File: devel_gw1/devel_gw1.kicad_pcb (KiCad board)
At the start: 4 copper layers, 50.8 x 95.2 mm, 179 parts, among them Q1 2N7002, Q10 2N7002, Q11 2N7002, Q12 2N7002, Q13 2N7002, Q14 2N7002, Q15 2N7002, Q16 2N7002, Q17 2N7002, Q18 2N7002, Q19 2N7002, Q2 2N7002, Q20 2N7002, Q21 2N7002, Q22 2N7002, Q23 2N7002, Q24 2N7002, Q25 2N7002, Q26 2N7002, Q27 2N7002, Q28 2N7002, Q29 2N7002, Q3 2N7002, Q30 2N7002, Q31 2N7002, Q32 2N7002, Q33 2N7002, Q34 2N7002, Q35 2N7002, Q36 2N7002, Q37 2N7002, Q38 2N7002, Q39 2N7002, Q4 2N7002, Q41 2N7002, Q5 2N7002, Q6 2N7002, Q7 2N7002, Q8 2N7002, Q9 2N7002, U1 GW1N-LV9QN88C6_I5_, U2 LM3480-3.3, U3 AP2202K-ADJ, U4 ESP-PSRAM32, U5 AT25SF081-XMHF-X, U6 AP62150Z6, X1 ASE-xxxMHz

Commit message: Devel board is production ready
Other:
- copper layers 4 -> 2
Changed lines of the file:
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@@
   (layers
     (0 "F.Cu" signal)
-    (1 "In1.Cu" mixed)
-    (2 "In2.Cu" mixed)
     (31 "B.Cu" signal)
     (32 "B.Adhes" user "B.Adhesive")
@@
       (layer "F.Mask" (type "Top Solder Mask") (thickness 0.01))
       (layer "F.Cu" (type "copper") (thickness 0.035))
-      (layer "dielectric 1" (type "core") (thickness 0.48) (material "FR4") (epsilon_r 4.5) (loss_tangent 0.02))
-      (layer "In1.Cu" (type "copper") (thickness 0.035))
-      (layer "dielectric 2" (type "prepreg") (thickness 0.48) (material "FR4") (epsilon_r 4.5) (loss_tangent 0.02))
-      (layer "In2.Cu" (type "copper") (thickness 0.035))
-      (layer "dielectric 3" (type "core") (thickness 0.48) (material "FR4") (epsilon_r 4.5) (loss_tangent 0.02))
+      (layer "dielectric 1" (type "core") (thickness 1.51) (material "FR4") (epsilon_r 4.5) (loss_tangent 0.02))
       (layer "B.Cu" (type "copper") (thickness 0.035))
       (layer "B.Mask" (type "Bottom Solder Mask") (thickness 0.01))
@@
     (grid_origin 144.7 83.3)
     (pcbplotparams
-      (layerselection 0x00010fc_ffffffff)
+      (layerselection 0x00010e0_ffffffff)
       (plot_on_all_layers_selection 0x0000000_00000000)
       (disableapertmacros false)
@@
       (outputformat 1)
       (mirror false)
-      (drillshape 1)
+      (drillshape 0)
       (scaleselection 1)
-      (outputdirectory "")
+      (outputdirectory "release-v1/")
     )
   )
@@
     (fp_line (start 1 0.625) (end -1 0.625)
       (stroke (width 0.1) (type solid)) (layer "F.Fab"))
-    (pad "1" smd roundrect (at -1.0375 0 180) (size 1.175 1.45) (layers "F.Cu" "F.Paste" "F.Mask") (roundrect_rratio 0.212766)
+    (pad "1" smd roundrect (at -1.0375 0 180) (size 1.175 1.45) (layers "F.Cu" "F.Paste" "F.Mask") (roundrect_rratio 0.2127659574)
       (net 129 "/V_IN") (pintype "passive"))
-    (pad "2" smd roundrect (at 1.0375 0 180) (size 1.175 1.45) (layers "F.Cu" "F.Paste" "F.Mask") (roundrect_rratio 0.212766)
+    (pad "2" smd roundrect (at 1.0375 0 180) (size 1.175 1.45) (layers "F.Cu" "F.Paste" "F.Mask") (roundrect_rratio 0.2127659574)
       (net 1 "GND") (pintype "passive"))
     (model "${KICAD6_3DMODEL_DIR}/Capacitor_SMD.3dshapes/C_0805_2012Metric.wrl"
@@
     (fp_line (start 1 0.625) (end -1 0.625)
       (stroke (width 0.1) (type solid)) (layer "F.Fab"))
-    (pad "1" smd roundrect (at -1.0375 0 270) (size 1.175 1.45) (layers "F.Cu" "F.Paste" "F.Mask") (roundrect_rratio 0.212766)
+    (pad "1" smd roundrect (at -1.0375 0 270) (size 1.175 1.45) (layers "F.Cu" "F.Paste" "F.Mask") (roundrect_rratio 0.2127659574)
       (net 117 "Net-(JP3-A)") (pintype "passive"))
-    (pad "2" smd roundrect (at 1.0375 0 270) (size 1.175 1.45) (layers "F.Cu" "F.Paste" "F.Mask") (roundrect_rratio 0.212766)
+    (pad "2" smd roundrect (at 1.0375 0 270) (size 1.175 1.45) (layers "F.Cu" "F.Paste" "F.Mask") (roundrect_rratio 0.2127659574)
       (net 1 "GND") (pintype "passive"))
     (model "${KICAD6_3DMODEL_DIR}/Capacitor_SMD.3dshapes/C_0805_2012Metric.wrl"
@@
     (fp_line (start 1.25 1) (end -1.25 1)
       (stroke (width 0.1) (type solid)) (layer "F.Fab"))
-    (pad "1" smd roundrect (at -1.1625 0 90) (size 1.425 2.2) (layers "F.Cu" "F.Paste" "F.Mask") (roundrect_rratio 0.175439)
+    (pad "1" smd roundrect (at -1.1625 0 90) (size 1.425 2.2) (layers "F.Cu" "F.Paste" "F.Mask") (roundrect_rratio 0.1754392982)
       (net 116 "Net-(U6-SW)") (pintype "passive"))
-    (pad "2" smd roundrect (at 1.1625 0 90) (size 1.425 2.2) (layers "F.Cu" "F.Paste" "F.Mask") (roundrect_rratio 0.175439)
+    (pad "2" smd roundrect (at 1.1625 0 90) (size 1.425 2.2) (layers "F.Cu" "F.Paste" "F.Mask") (roundrect_rratio 0.1754392982)
       (net 117 "Net-(JP3-A)") (pintype "passive"))
     (model "${KICAD6_3DMODEL_DIR}/Inductor_SMD.3dshapes/L_1008_2520Metric.wrl"
@@
     (fp_line (start 1 0.625) (end -1 0.625)
       (stroke (width 0.1) (type solid)) (layer "F.Fab"))
-    (pad "1" smd roundrect (at -1.0375 0 270) (size 1.175 1.45) (layers "F.Cu" "F.Paste" "F.Mask") (roundrect_rratio 0.212766)
+    (pad "1" smd roundrect (at -1.0375 0 270) (size 1.175 1.45) (layers "F.Cu" "F.Paste" "F.Mask") (roundrect_rratio 0.2127659574)
       (net 117 "Net-(JP3-A)") (pintype "passive"))
-    (pad "2" smd roundrect (at 1.0375 0 270) (size 1.175 1.45) (layers "F.Cu" "F.Paste" "F.Mask") (roundrect_rratio 0.212766)
+    (pad "2" smd roundrect (at 1.0375 0 270) (size 1.175 1.45) (layers "F.Cu" "F.Paste" "F.Mask") (roundrect_rratio 0.2127659574)
       (net 1 "GND") (pintype "passive"))
     (model "${KICAD6_3DMODEL_DIR}/Capacitor_SMD.3dshapes/C_0805_2012Metric.wrl"

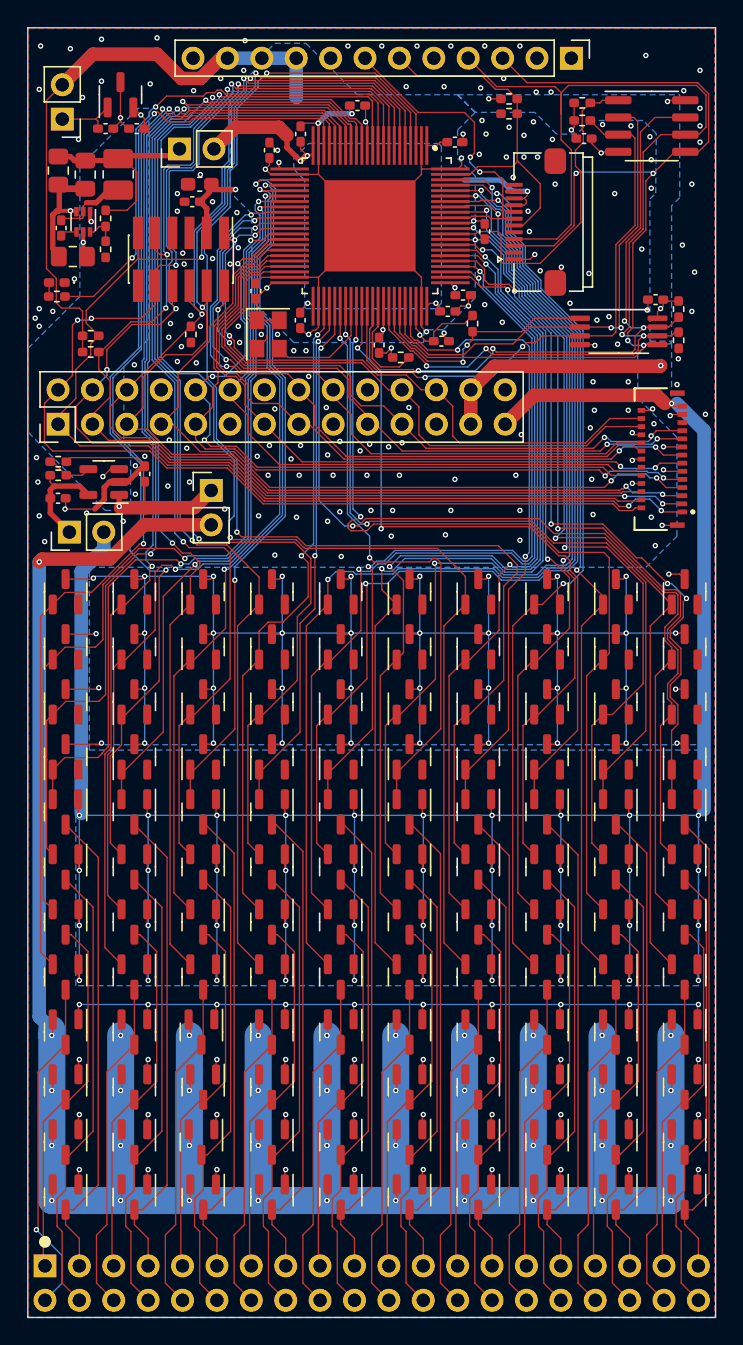
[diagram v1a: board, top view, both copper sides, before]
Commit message: Added power input connector
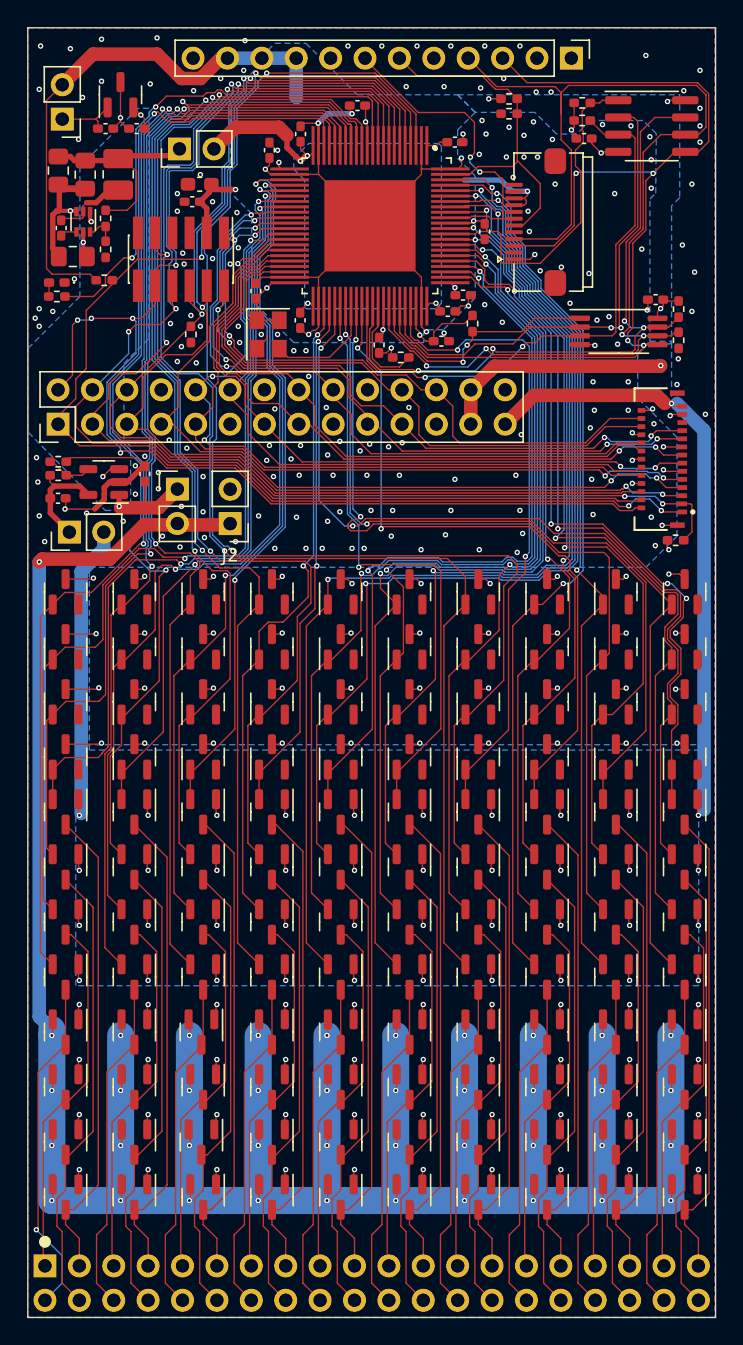
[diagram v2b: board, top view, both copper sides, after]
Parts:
- added J2: Conn_01x02, Connector_PinHeader_2.54mm:PinHeader_1x02_P2.54mm_Vertical, F.Cu at (138.9, 109.8)
- moved R7 45.4 mm to (171.8, 111.0)
- moved R16 4.22 mm to (129.6, 91.8)
- moved JP4 2.50 mm to (135.0, 107.2)
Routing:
- net +5V: track 284.2 -> 115.8 mm
- net +3V3: track 285.6 -> 141.5 mm, vias 57 -> 58
- net GND: track 172.4 -> 126.4 mm, vias 219 -> 229
- net /RECONFIG_N: track 93.2 -> 96.1 mm
- net /V_IN: track 15.5 -> 13.0 mm
- net /PIN27_F: track 96.9 -> 98.3 mm
- net /JTAG_TDI: track 97.5 -> 98.7 mm, vias 4 -> 6
- net LINE: track 265.6 -> 266.8 mm
- net /PIN36_F: track 80.7 -> 81.6 mm
- net /PIN35_F: track 76.6 -> 75.8 mm
- net /JTAG_SEL_N: track 100.1 -> 99.4 mm
- net /PIN28_F: track 101.8 -> 102.5 mm
- net /PIN29_F: track 65.1 -> 64.5 mm
- net /PIN9_F: track 65.6 -> 65.0 mm
- net /PIN32_F: track 80.9 -> 80.3 mm
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
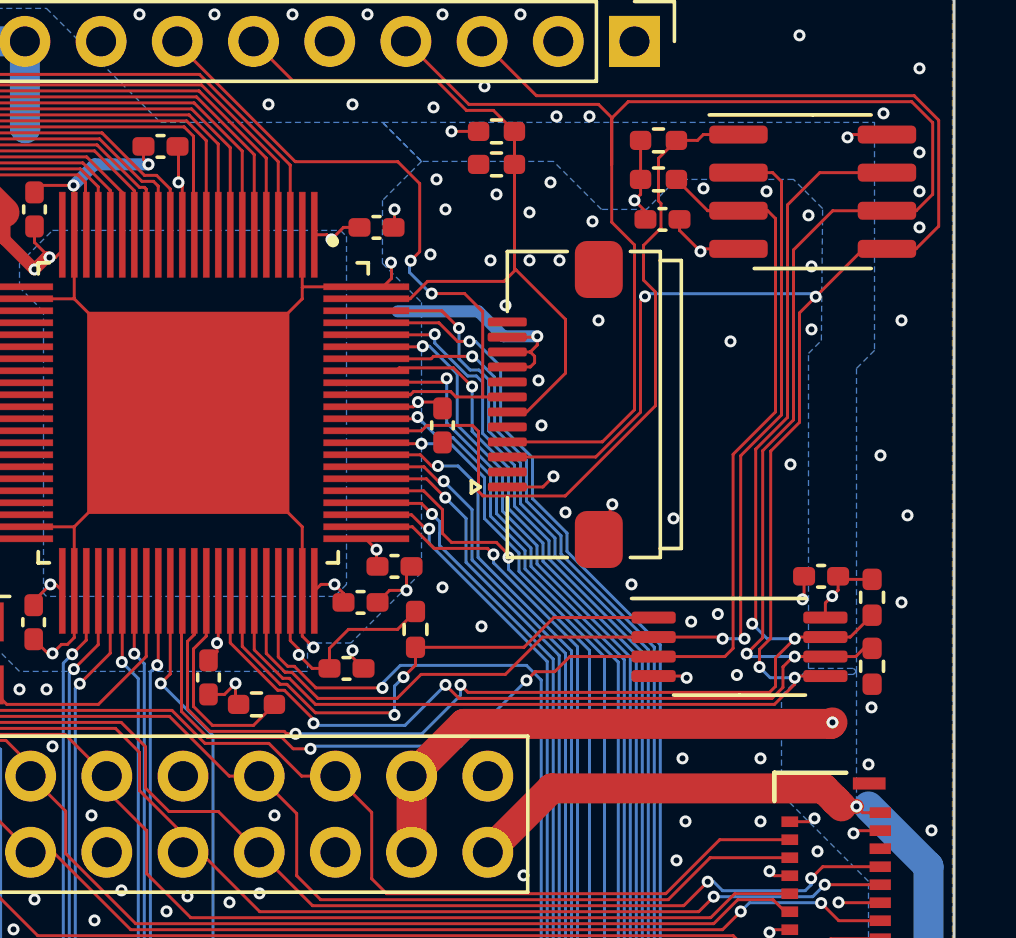
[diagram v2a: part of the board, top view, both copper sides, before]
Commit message: Replaced TSSOP FLASH with SO-8 one due to availability concerns.
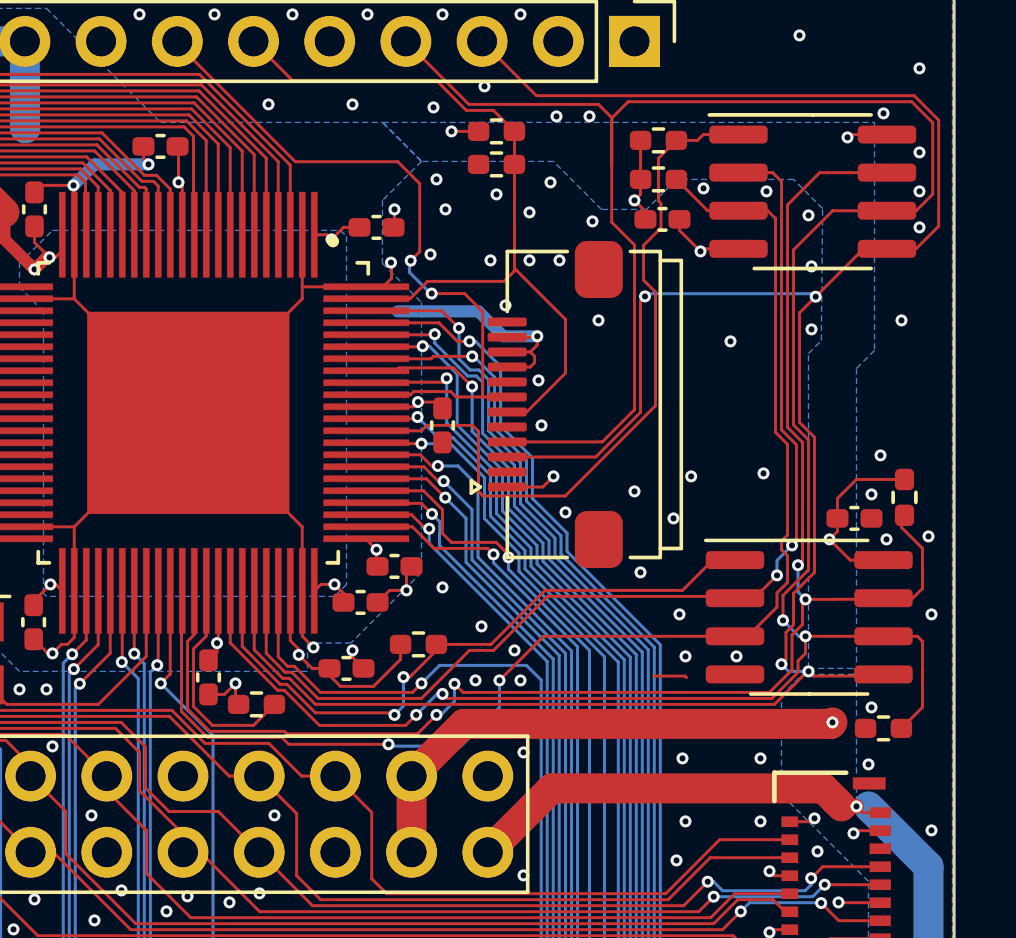
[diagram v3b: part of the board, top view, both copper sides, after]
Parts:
- removed U5: AT25SF081-XMHF-X, Package_SO:TSSOP-8_4.4x3mm_P0.65mm
- added U7: AT25SF081-SSHD-X, Package_SO:SOIC-8_3.9x4.9mm_P1.27mm, F.Cu at (169.9, 94.6)
- moved R10 3.50 mm to (173.1, 90.6)
- moved C14 2.23 mm to (171.4, 91.3), turned to 0 degrees
- moved R11 2.10 mm to (172.4, 98.3), turned to 180 degrees
- moved R9 0.51 mm to (156.9, 95.5), turned to 0 degrees
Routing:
- net /SPI_CLK: track 83.8 -> 86.8 mm
- net +3V3: track 141.5 -> 144.3 mm
- net /SPI_IO3: track 48.6 -> 51.4 mm
- net GND: track 126.4 -> 124.0 mm, vias 229 -> 234
- net /FLASH_CS_N: track 17.8 -> 20.1 mm
- net /SPI_MOSI_IO0: track 75.5 -> 77.0 mm
- net /SPI_IO2: track 42.0 -> 43.0 mm

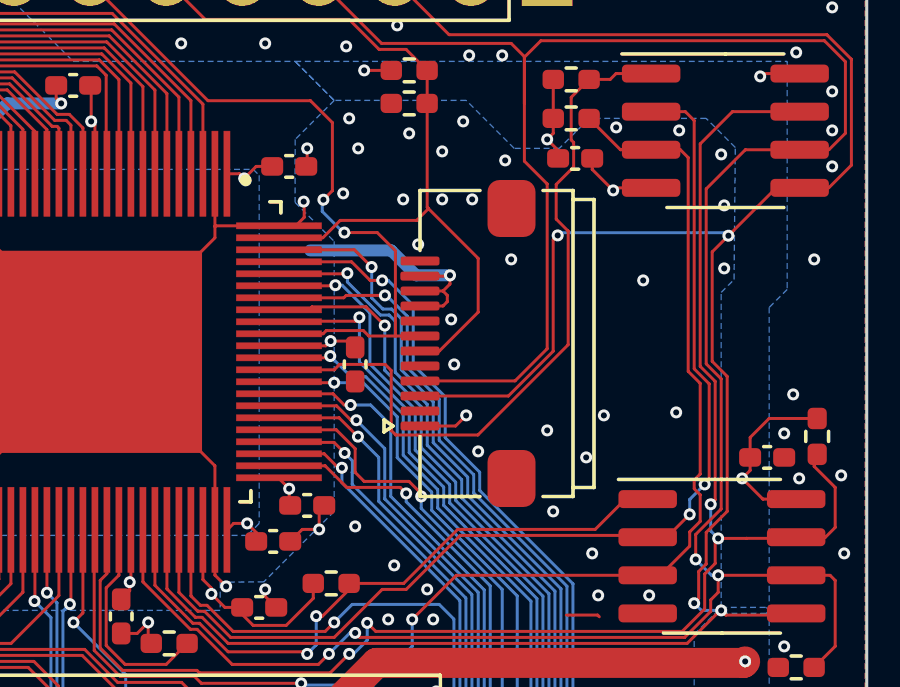
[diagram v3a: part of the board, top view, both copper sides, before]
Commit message: Populated part numbers for most parts.
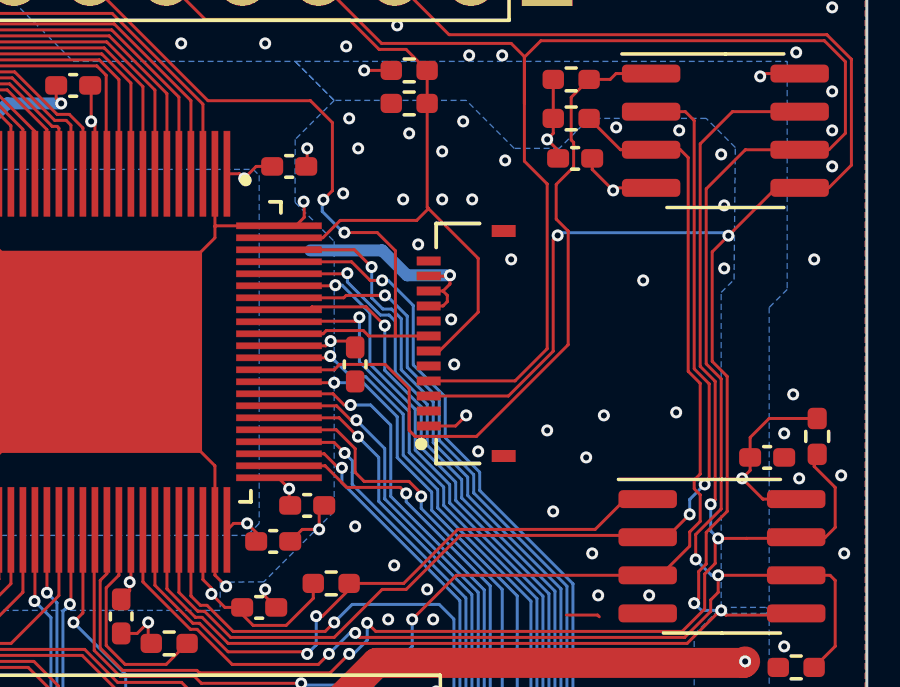
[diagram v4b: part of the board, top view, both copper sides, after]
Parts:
- J_DISPLAY1: footprint UNIC:CF31121D0R0-05-NH -> UNIC:HRS_FH19C-12S-0.5SH_05_
- U4: value ESP-PSRAM32 -> APS6404L-3SQR-ZR
- moved J_DISPLAY1 0.29 mm to (160.2, 87.5)

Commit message: Ready to roll with DEVEL board!
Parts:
- added J_DISPLAY3: Conn_01x12_MountingPin, UNIC:CF31121D0R0-05-NH, F.Cu at (160.0, 87.5)
- C1, C10, C11, C13, C14, C15, C16, C17, C18, C19, C2, C20, C21, C22, C23, C4, C6, C9: value 0.1u -> 2.2u
- C12: footprint Capacitor_SMD:C_0603_1608Metric_Pad1.08x0.95mm_HandSolder -> Capacitor_SMD:C_0805_2012Metric_Pad1.18x1.45mm_HandSolder
- J_DISPLAY1: footprint UNIC:HRS_FH19C-12S-0.5SH_05_ -> UNIC:CF4212FH0R0-05-NH; moved to B.Cu
- L1: value 3.3uH -> 10uH
- U4: value APS6404L-3SQR-ZR -> APS6404L-3SQR-SN
- U7: value AT25SF081-SSHD-X -> AT25SF081-SSHB-X
- X1: value ASE-xxxMHz -> 27MHz
- moved R16 26.6 mm to (152.6, 78.4), turned to 180 degrees
- moved R10 13.8 mm to (170.6, 77.0), turned to 0 degrees
- moved C4 6.04 mm to (140.8, 82.2), turned to -90 degrees
- moved J_DISPLAY1 1.17 mm to (161.3, 87.5), turned to -90 degrees
- moved C12 0.61 mm to (136.5, 85.3)
- moved C7 0.30 mm to (126.2, 84.0)
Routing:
- net +3V3: track 144.3 -> 131.4 mm, vias 58 -> 61
- net GND: track 124.0 -> 117.0 mm, vias 234 -> 248
- net /LCD_CS_N: track 22.8 -> 26.8 mm, vias 2 -> 3
- net /SPI_MOSI_IO0: track 77.0 -> 74.1 mm, vias 4 -> 5
- net /SPI_CLK: track 86.8 -> 84.4 mm, vias 4 -> 5
- net /PIN27_F: track 98.3 -> 99.4 mm
- net /SPI_IO3: track 51.4 -> 50.5 mm
- net /PIN20_F: track 52.0 -> 51.1 mm
- net /LCD_RST_N: track 25.6 -> 26.2 mm, vias 0 -> 1
- net Net-(JP3-A): track 14.3 -> 13.7 mm
- net /PIN30_F: track 70.3 -> 69.7 mm
- net /PIN21_F: track 57.4 -> 56.9 mm
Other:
- board text added: "(C) 2024 Andras Tantos & Modular Circuits"
- board text added: "UnIC development board"
